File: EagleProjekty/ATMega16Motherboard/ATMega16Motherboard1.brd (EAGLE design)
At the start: 100 x 80 mm, 27 parts, among them IC2 7805T, IC3 MEGA16-P, Q1 12Mhz, Q2 12Mhz, Q3 12Mhz, Q4 12Mhz

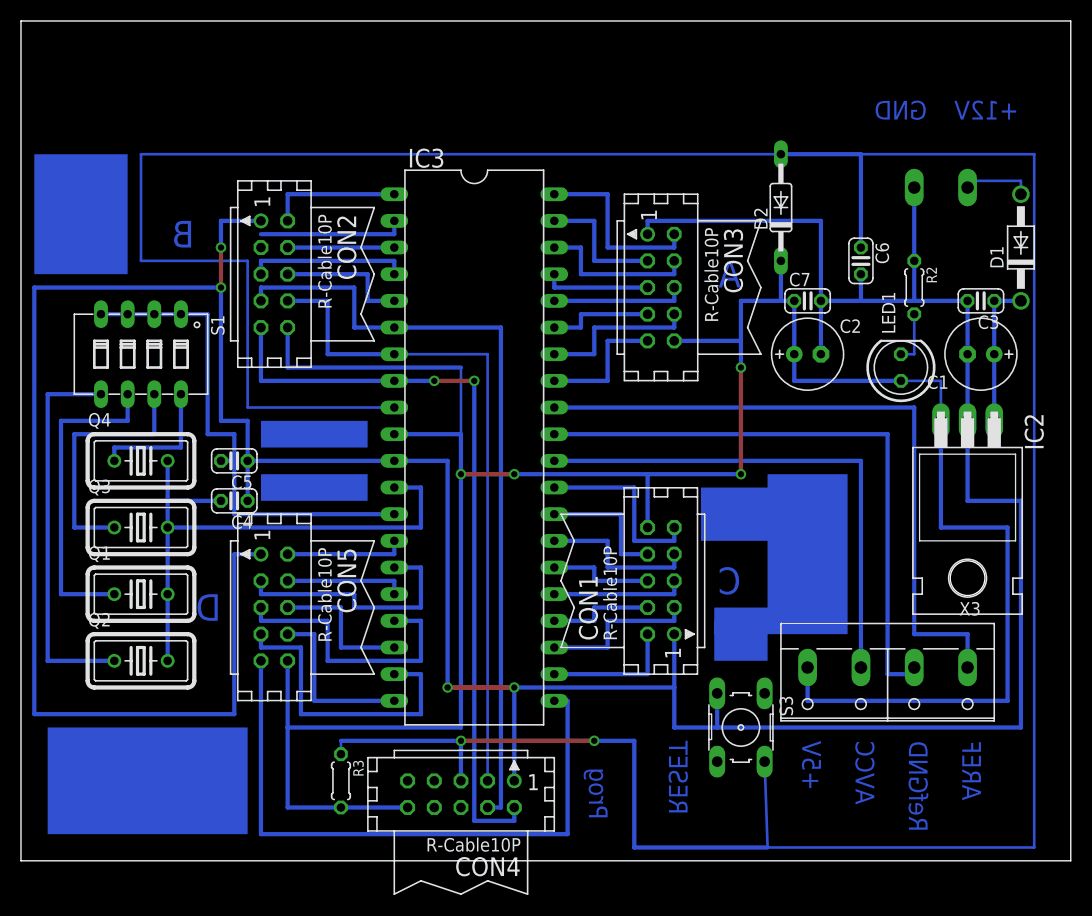
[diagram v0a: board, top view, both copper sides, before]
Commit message: Update motherboard AT Mega 16
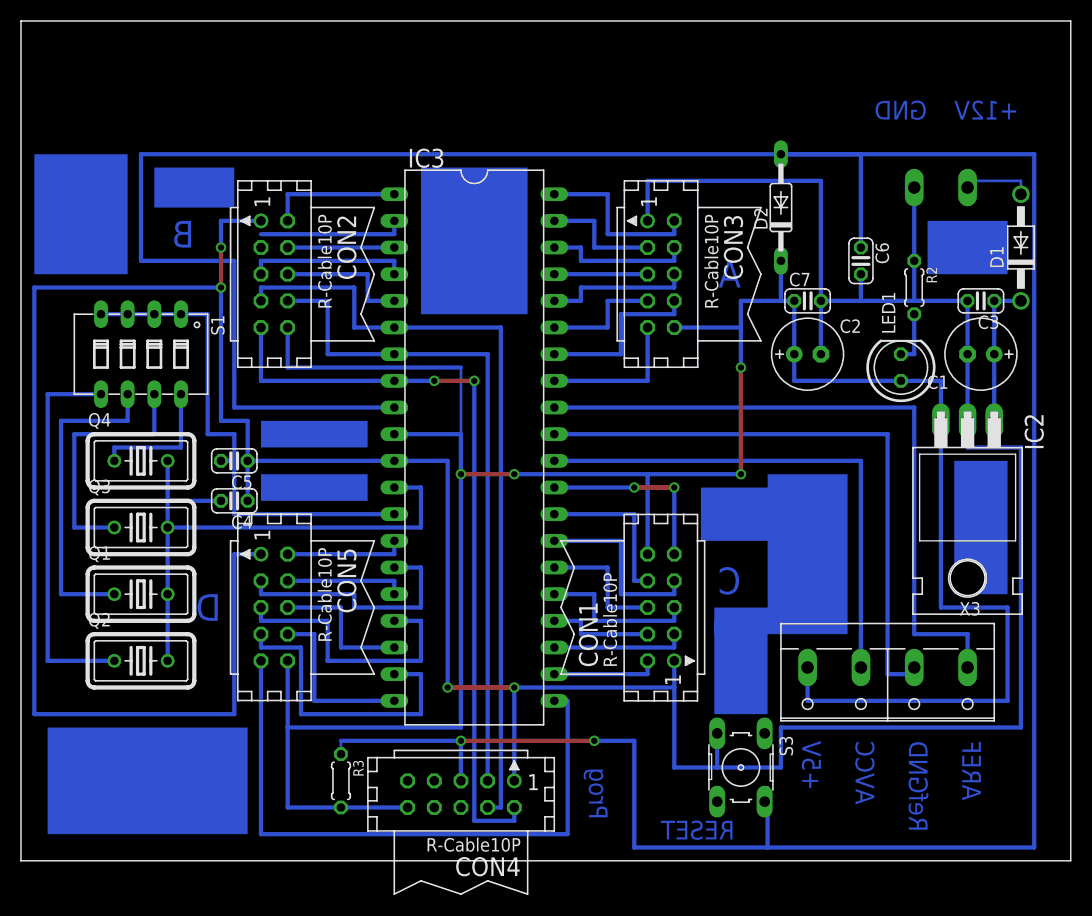
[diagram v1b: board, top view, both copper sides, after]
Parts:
- moved S3 3.81 mm to (68.6, 8.89)
- moved CON1 2.54 mm to (61.0, 24.1)
- moved CON3 1.27 mm to (61.0, 55.9)
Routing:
- net GND: track 348.1 -> 359.5 mm
- net N$30: track 297.7 -> 304.1 mm
- net N$40: track 15.2 -> 17.8 mm
- net N$39: track 10.2 -> 12.7 mm
- net N$6: track 15.2 -> 12.7 mm
- net N$41: track 12.7 -> 15.2 mm
- net N$3: track 12.7 -> 10.2 mm
- net N$38: track 12.7 -> 15.2 mm
- net +5V: track 247.0 -> 249.6 mm
- net N$36: track 15.2 -> 16.5 mm
- net N$34: track 10.2 -> 11.4 mm
- net N$33: track 12.7 -> 14.0 mm
- net N$32: track 10.2 -> 8.89 mm
- net N$19: track 12.7 -> 11.4 mm
- net N$37: track 12.7 -> 14.0 mm
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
